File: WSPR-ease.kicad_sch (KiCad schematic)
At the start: 31 parts, among them J1 GNSS Ant, J2 Tx Ant, J3 USB_C_16P_Stacked, Q1 MMBF170, U1 ESP32-S3-WROOM-1, U2 NCP1117-3.3_SOT223, U3 ATGM336H-5N31

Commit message: Minor tweaks after submitting 001 build to pcbway
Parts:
- BT1: value CR1220 -> S8401-46; footprint Battery:Battery_Panasonic_CR1220-VCN_Vertical_CircularHoles -> S8401-46; symbol Device:Battery_Cell -> Library:S8401-46; LCSC (none) -> C5904513; Manufacturer_Name (none) -> Harwin; Manufacturer_Part_Number (none) -> S8401-46; Mouser Part Number (none) -> 855-S8401-46; Mouser Price/Stock (none) -> https://www.mouser.co.uk/ProductDetail/Harwin/S8401-46?qs=Q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
- C1: footprint Capacitor_SMD:C_0805_2012Metric -> Capacitor_SMD:C_0603_1608Metric
- C10: MFG Vishay -> (none); MPN MAL215097011E3 -> (none); Manufacturer_Name (none) -> Vishay; Mouser Part Number (none) -> MAL215097011E3
- J1, J2: LCSC (none) -> C496551
- J3: LCSC (none) -> C165948; MFG Korean Hroparts -> (none); MPN TYPE-C-31-M-12 -> (none); Manufacturer_Name (none) -> Korean Hroparts; Mouser Part Number (none) -> TYPE-C-31-M-12
- Q1: LCSC (none) -> C28871
- U1: value ESP32-S3-WROOM-1 -> ESP32-S3-WROOM-1-N8R8; LCSC (none) -> C2913204; Manufacturer_Name (none) -> Espressif; Mouser Part Number (none) -> ESP32-S3-WROOM-1-N8R8
- U3: LCSC (none) -> C90770
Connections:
- net GND: now also BT1.1 (-VE); no longer BT1.2 (-)
- net at U3.6 (V_BCKP): now also BT1.2, BT1.3; no longer BT1.1 (+)
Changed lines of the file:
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@@
 	)
 	(junction
+		(at 118.11 33.02)
+		(diameter 0)
+		(color 0 0 0 0)
+	)
+	(junction
 		(at 137.16 78.74)
 		(diameter 0)
@@
 	(wire
 		(pts
-			(xy 128.27 33.02) (xy 128.27 34.29)
+			(xy 143.51 33.02) (xy 143.51 34.29)
 		)
 		(stroke
@@
 	(wire
 		(pts
+			(xy 118.11 30.48) (xy 118.11 33.02)
+		)
+		(stroke
+			(width 0)
+			(type default)
+		)
+	)
+	(wire
+		(pts
 			(xy 88.9 63.5) (xy 90.17 63.5)
 		)
@@
 	(wire
 		(pts
+			(xy 119.38 30.48) (xy 118.11 30.48)
+		)
+		(stroke
+			(width 0)
+			(type default)
+		)
+	)
+	(wire
+		(pts
 			(xy 143.51 195.58) (xy 143.51 196.85)
 		)
@@
 	(wire
 		(pts
-			(xy 127 33.02) (xy 128.27 33.02)
+			(xy 142.24 33.02) (xy 143.51 33.02)
 		)
 		(stroke
@@
 			)
 		)
-		(property "Footprint" "Capacitor_SMD:C_0805_2012Metric"
+		(property "Footprint" "Capacitor_SMD:C_0603_1608Metric"
 			(at 32.7152 87.63 0)
 			(effects
@@
 	)
 	(symbol
-		(lib_id "Device:Battery_Cell")
-		(at 124.46 33.02 90)
+		(lib_id "Library:S8401-46")
+		(at 119.38 33.02 0)
 		(mirror x)
 		(unit 1)
@@
 		(fields_autoplaced yes)
 		(property "Reference" "BT1"
-			(at 122.6185 25.4 90)
+			(at 130.81 22.86 0)
 			(effects
 				(font
@@
 			)
 		)
-		(property "Value" "CR1220"
-			(at 122.6185 27.94 90)
+		(property "Value" "S8401-46"
+			(at 130.81 25.4 0)
 			(effects
 				(font
@@
 			)
 		)
-		(property "Footprint" "Battery:Battery_Panasonic_CR1220-VCN_Vertical_CircularHoles"
-			(at 122.936 33.02 90)
+		(property "Footprint" "S8401-46"
+			(at 138.43 -61.9 0)
 			(effects
 				(font
 					(size 1.27 1.27)
 				)
+				(justify left top)
 				(hide yes)
 			)
 		)
-		(property "Datasheet" "~"
-			(at 122.936 33.02 90)
+		(property "Datasheet" "https://cdn.harwin.com/pdfs/S8401.pdf"
+			(at 138.43 -161.9 0)
 			(effects
 				(font
 					(size 1.27 1.27)
 				)
+				(justify left top)
 				(hide yes)
 			)
 		)
-		(property "Description" "Single-cell battery"
-			(at 124.46 33.02 0)
+		(property "Description" "Coin Cell Battery Retainer, Vertical Throughboard, for CR2032 and BR2032 Coin Cell Batteries"
+			(at 119.38 33.02 0)
 			(effects
 				(font
@@
 			)
 		)
-		(property "LCSC" ""
-			(at 124.46 33.02 90)
+		(property "LCSC" "C5904513"
+			(at 119.38 33.02 90)
+			(effects
+				(font
+					(size 1.27 1.27)
+				)
+				(hide yes)
+			)
+		)
+		(property "Height" ""
+			(at 138.43 -361.9 0)
+			(effects
+				(font
+					(size 1.27 1.27)
+				)
+				(justify left top)
+				(hide yes)
+			)
+		)
+		(property "Mouser Part Number" "855-S8401-46"
+			(at 138.43 -461.9 0)
+			(effects
+				(font
+					(size 1.27 1.27)
+				)
+				(justify left top)
+				(hide yes)
+			)
+		)
+		(property "Mouser Price/Stock" "https://www.mouser.co.uk/ProductDetail/Harwin/S8401-46?qs=Qom7kyPojXaFNoCO9lxVnA%3D%3D"
+			(at 138.43 -561.9 0)
+			(effects
+				(font
+					(size 1.27 1.27)
+				)
+				(justify left top)
+				(hide yes)
+			)
+		)
+		(property "Manufacturer_Name" "Harwin"
+			(at 138.43 -661.9 0)
+			(effects
+				(font
+					(size 1.27 1.27)
+				)
+				(justify left top)
+				(hide yes)
+			)
+		)
+		(property "Manufacturer_Part_Number" "S8401-46"
+			(at 138.43 -761.9 0)
 			(effects
 				(font
 					(size 1.27 1.27)
 				)
+				(justify left top)
 				(hide yes)
 			)
@@
 		(pin "1"
 		)
+		(pin "3"
+		)
 		(instances
 			(project ""
@@
 			)
 		)
-		(property "MFG" "Korean Hroparts"
+		(property "MFG" ""
 			(at 227.33 66.04 0)
 			(effects
@@
 			)
 		)
-		(property "MPN" "TYPE-C-31-M-12"
+		(property "MPN" ""
 			(at 227.33 66.04 0)
 			(effects
@@
 			)
 		)
-		(property "LCSC" ""
+		(property "LCSC" "C165948"
+			(at 227.33 66.04 0)
+			(effects
+				(font
+					(size 1.27 1.27)
+				)
+				(hide yes)
+			)
+		)
+		(property "Manufacturer_Name" "Korean Hroparts"
+			(at 227.33 66.04 0)
+			(effects
+				(font
+					(size 1.27 1.27)
+				)
+				(hide yes)
+			)
+		)
+		(property "Mouser Part Number" "TYPE-C-31-M-12"
 			(at 227.33 66.04 0)
 			(effects
@@
 			)
 		)
-		(property "LCSC" ""
+		(property "LCSC" "C28871"
 			(at 41.91 76.2 0)
 			(effects
@@
 			)
 		)
-		(property "LCSC" ""
+		(property "LCSC" "C90770"
 			(at 134.62 58.42 0)
 			(effects
@@
 			)
 		)
-		(property "Datasheet" "~"
+		(property "Datasheet" "https://www.lcsc.com/datasheet/C496551.pdf"
 			(at 170.18 49.53 0)
 			(effects
@@
 			)
 		)
-		(property "Description" "small coaxial connector (BNC, SMA, SMB, SMC, Cinch/RCA, LEMO, ...)"
+		(property "Description" "1 Inner Bore SMA Board Side Elbow 50Ω 5.3mm Through Hole Coaxial Connector (RF) Assemblies RoHS"
 			(at 170.18 49.53 0)
 			(effects
@@
 			)
 		)
-		(property "LCSC" ""
+		(property "LCSC" "C496551"
 			(at 170.18 49.53 0)
 			(effects
@@
 			)
 		)
-		(property "Value" "ESP32-S3-WROOM-1"
+		(property "Value" "ESP32-S3-WROOM-1-N8R8"
 			(at 75.8033 48.26 0)
 			(effects
@@
 			)
 		)
-		(property "LCSC" ""
+		(property "LCSC" "C2913204"
+			(at 73.66 76.2 0)
+			(effects
+				(font
+					(size 1.27 1.27)
+				)
+				(hide yes)
+			)
+		)
+		(property "Manufacturer_Name" "Espressif"
+			(at 73.66 76.2 0)
+			(effects
+				(font
+					(size 1.27 1.27)
+				)
+				(hide yes)
+			)
+		)
+		(property "Mouser Part Number" "ESP32-S3-WROOM-1-N8R8"
 			(at 73.66 76.2 0)
 			(effects
@@
 			)
 		)
-		(property "Datasheet" "~"
+		(property "Datasheet" "https://www.lcsc.com/datasheet/C496551.pdf"
 			(at 195.58 142.24 0)
 			(effects
@@
 			)
 		)
-		(property "Description" "small coaxial connector (BNC, SMA, SMB, SMC, Cinch/RCA, LEMO, ...)"
+		(property "Description" "1 Inner Bore SMA Board Side Elbow 50Ω 5.3mm Through Hole Coaxial Connector (RF) Assemblies RoHS"
 			(at 195.58 142.24 0)
 			(effects
@@
 			)
 		)
-		(property "LCSC" ""
+		(property "LCSC" "C496551"
 			(at 195.58 142.24 0)
 			(effects
@@
 	(symbol
 		(lib_id "power:GND")
-		(at 128.27 34.29 0)
+		(at 143.51 34.29 0)
 		(unit 1)
 		(exclude_from_sim no)
@@
 		(fields_autoplaced yes)
 		(property "Reference" "#PWR012"
-			(at 128.27 40.64 0)
+			(at 143.51 40.64 0)
 			(effects
 				(font
@@
 		)
 		(property "Value" "GND"
-			(at 128.27 39.37 0)
+			(at 143.51 39.37 0)
 			(effects
 				(font
@@
 		)
 		(property "Footprint" ""
-			(at 128.27 34.29 0)
+			(at 143.51 34.29 0)
 			(effects
 				(font
@@
 		)
 		(property "Datasheet" ""
-			(at 128.27 34.29 0)
+			(at 143.51 34.29 0)
 			(effects
 				(font
@@
 		)
 		(property "Description" "Power symbol creates a global label with name \"GND\" , ground"
-			(at 128.27 34.29 0)
+			(at 143.51 34.29 0)
 			(effects
 				(font
@@
 			)
 		)
-		(property "MFG" "Vishay"
+		(property "MFG" ""
+			(at 262.89 63.5 0)
+			(effects
+				(font
+					(size 1.27 1.27)
+				)
+				(hide yes)
+			)
+		)
+		(property "MPN" ""
+			(at 262.89 63.5 0)
+			(effects
+				(font
+					(size 1.27 1.27)
+				)
+				(hide yes)
+			)
+		)
+		(property "Manufacturer_Name" "Vishay"
 			(at 262.89 63.5 0)
 			(effects
@@
 			)
 		)
-		(property "MPN" "MAL215097011E3"
+		(property "Mouser Part Number" "MAL215097011E3"
 			(at 262.89 63.5 0)
 			(effects

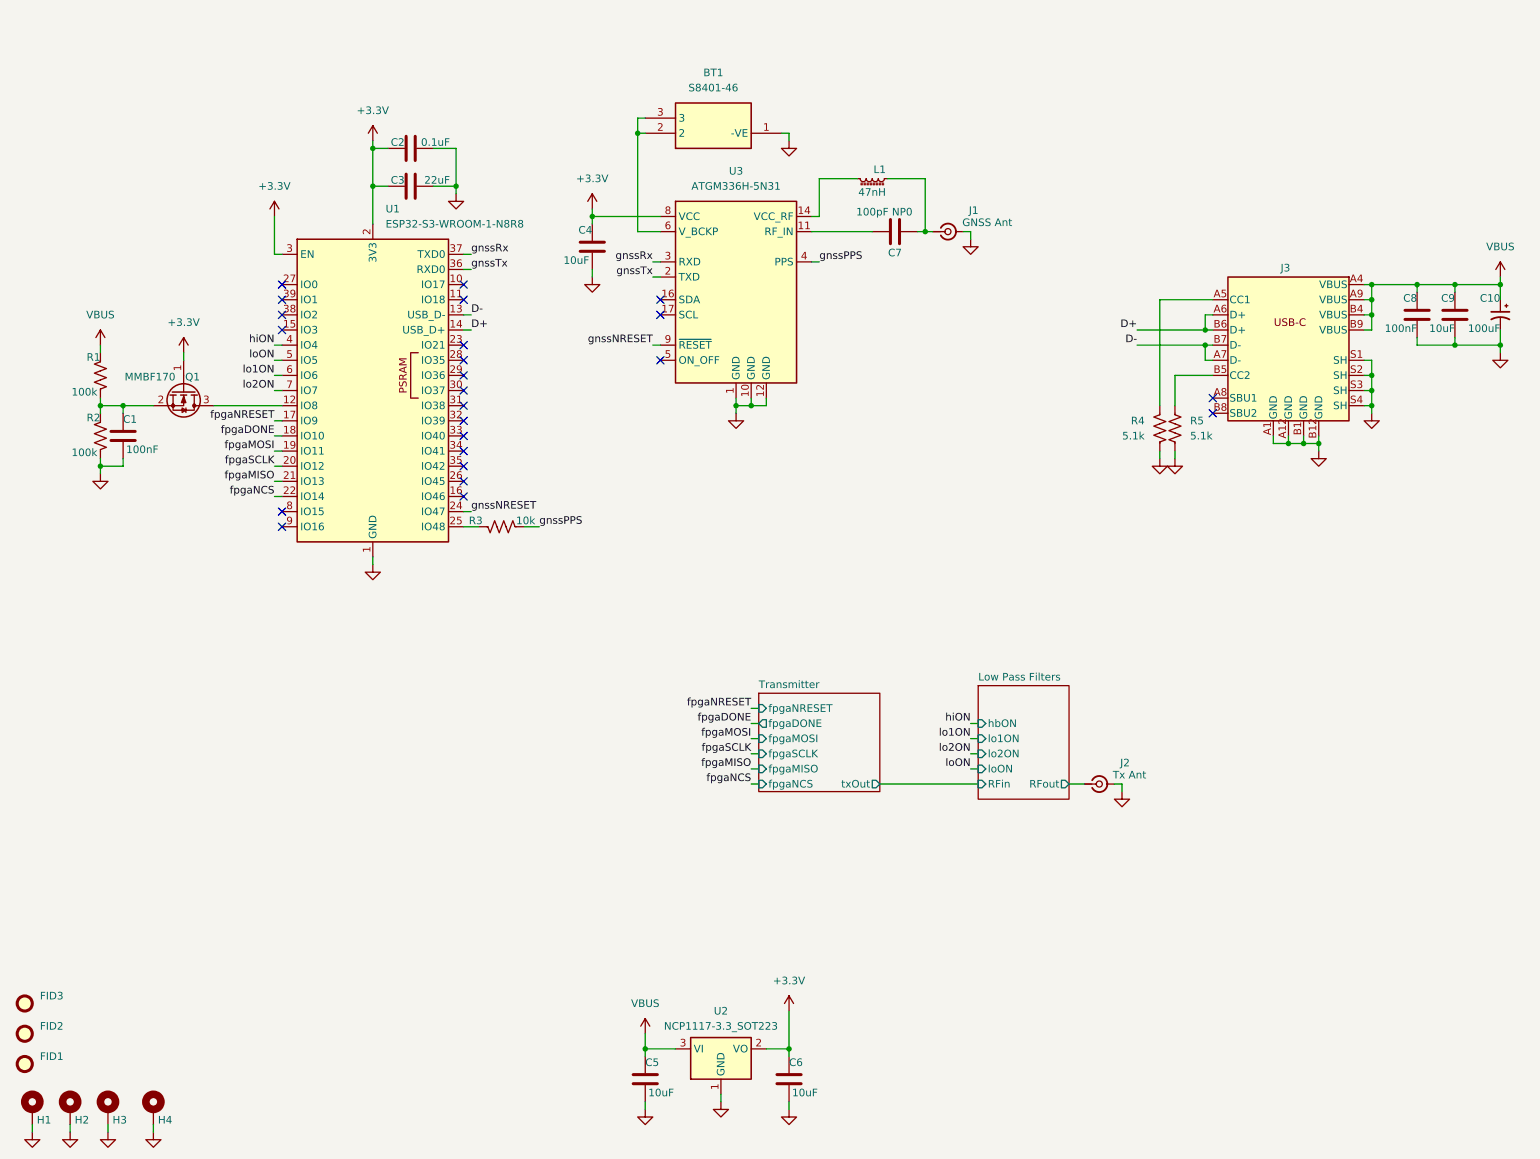
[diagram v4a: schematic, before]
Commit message: Submitted to PCBway (I had to update BOM after oops)
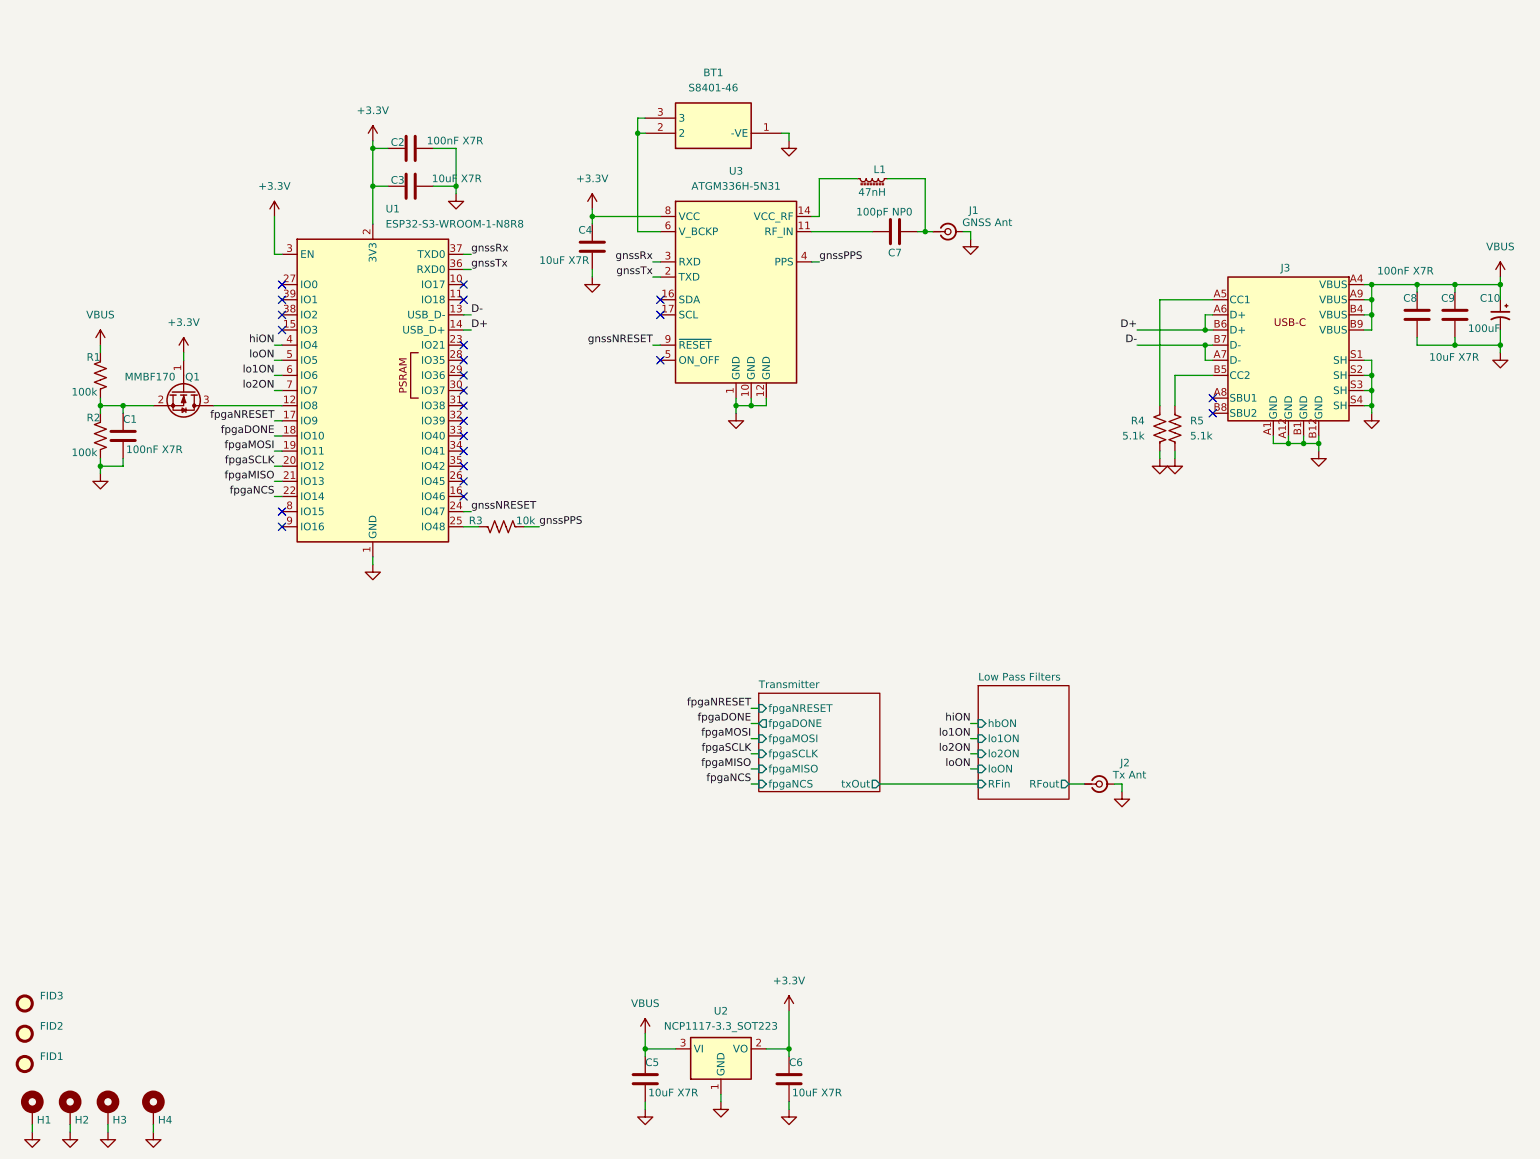
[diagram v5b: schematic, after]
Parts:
- C1, C8: value 100nF -> 100nF X7R; LCSC (none) -> C14663
- C2: value 0.1uF -> 100nF X7R; LCSC (none) -> C14663
- C3: value 22uF -> 10uF X7R; LCSC (none) -> C19702
- C4, C5, C6, C9: value 10uF -> 10uF X7R; LCSC (none) -> C32635
- C7: LCSC (none) -> C14665
- FID1, FID2, FID3, H1, H2, H3, H4: LCSC (none) -> DNP
- L1: LCSC (none) -> C98076
- R1, R2: LCSC (none) -> C7311067
- R3: LCSC (none) -> C2930027
- R4, R5: LCSC (none) -> C2907114
- U2: LCSC (none) -> C26537
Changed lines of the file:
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@@
 			)
 		)
-		(property "Value" "100nF"
+		(property "Value" "100nF X7R"
 			(at 32.258 86.106 0)
 			(effects
@@
 			)
 		)
-		(property "LCSC" ""
+		(property "LCSC" "C14663"
 			(at 31.75 83.82 0)
 			(effects
@@
 			)
 		)
-		(property "LCSC" ""
+		(property "LCSC" "C7311067"
 			(at 27.94 73.66 0)
 			(effects
@@
 			)
 		)
+		(property "LCSC" "DNP"
+			(at 29.21 196.85 0)
+			(effects
+				(font
+					(size 1.27 1.27)
+				)
+				(hide yes)
+			)
+		)
 		(pin "1"
 		)
@@
 			)
 		)
-		(property "Value" "100nF"
-			(at 248.92 65.786 0)
+		(property "Value" "100nF X7R"
+			(at 251.714 56.134 0)
 			(effects
 				(font
@@
 			)
 		)
-		(property "LCSC" ""
+		(property "LCSC" "C14663"
 			(at 248.92 63.5 0)
 			(effects
@@
 			)
 		)
-		(property "LCSC" ""
+		(property "LCSC" "C14665"
 			(at 161.29 49.53 90)
 			(effects
@@
 			)
 		)
+		(property "LCSC" "DNP"
+			(at 16.51 196.85 0)
+			(effects
+				(font
+					(size 1.27 1.27)
+				)
+				(hide yes)
+			)
+		)
 		(pin "1"
 		)
@@
 			)
 		)
+		(property "LCSC" "DNP"
+			(at 15.24 189.23 0)
+			(effects
+				(font
+					(size 1.27 1.27)
+				)
+				(hide yes)
+			)
+		)
 		(instances
 			(project ""
@@
 			)
 		)
-		(property "Value" "10uF"
+		(property "Value" "10uF X7R"
 			(at 144.018 194.056 0)
 			(effects
@@
 			)
 		)
-		(property "LCSC" ""
+		(property "LCSC" "C32635"
 			(at 143.51 191.77 0)
 			(effects
@@
 			)
 		)
-		(property "LCSC" ""
+		(property "LCSC" "C98076"
 			(at 157.48 40.64 90)
 			(effects
@@
 			)
 		)
-		(property "LCSC" ""
+		(property "LCSC" "C26537"
 			(at 132.08 186.69 0)
 			(effects
@@
 			)
 		)
+		(property "LCSC" "DNP"
+			(at 36.83 196.85 0)
+			(effects
+				(font
+					(size 1.27 1.27)
+				)
+				(hide yes)
+			)
+		)
 		(pin "1"
 		)
@@
 			)
 		)
+		(property "LCSC" "DNP"
+			(at 15.24 179.07 0)
+			(effects
+				(font
+					(size 1.27 1.27)
+				)
+				(hide yes)
+			)
+		)
 		(instances
 			(project "WSPR-ease"
@@
 			)
 		)
-		(property "Value" "10uF"
-			(at 255.27 65.786 0)
+		(property "Value" "10uF X7R"
+			(at 259.334 70.612 0)
 			(effects
 				(font
@@
 			)
 		)
-		(property "LCSC" ""
+		(property "LCSC" "C32635"
 			(at 255.27 63.5 0)
 			(effects
@@
 			)
 		)
-		(property "LCSC" ""
+		(property "LCSC" "C2907114"
 			(at 208.28 82.55 0)
 			(effects
@@
 			)
 		)
-		(property "LCSC" ""
+		(property "LCSC" "C7311067"
 			(at 27.94 83.82 0)
 			(effects
@@
 			)
 		)
-		(property "Value" "10uF"
+		(property "Value" "10uF X7R"
 			(at 119.888 194.056 0)
 			(effects
@@
 			)
 		)
-		(property "LCSC" ""
+		(property "LCSC" "C32635"
 			(at 119.38 191.77 0)
 			(effects
@@
 			)
 		)
-		(property "LCSC" ""
+		(property "LCSC" "C2930027"
 			(at 95.25 99.06 90)
 			(effects
@@
 			)
 		)
-		(property "Value" "22uF"
-			(at 86.614 40.894 90)
+		(property "Value" "10uF X7R"
+			(at 91.948 40.64 90)
 			(effects
 				(font
@@
 			)
 		)
-		(property "LCSC" ""
+		(property "LCSC" "C19702"
 			(at 80.01 41.91 90)
 			(effects
@@
 			)
 		)
-		(property "Value" "0.1uF"
-			(at 86.614 34.544 90)
+		(property "Value" "100nF X7R"
+			(at 92.202 34.29 90)
 			(effects
 				(font
@@
 			)
 		)
-		(property "LCSC" ""
+		(property "LCSC" "C14663"
 			(at 80.01 35.56 90)
 			(effects
@@
 			)
 		)
+		(property "LCSC" "DNP"
+			(at 15.24 184.15 0)
+			(effects
+				(font
+					(size 1.27 1.27)
+				)
+				(hide yes)
+			)
+		)
 		(instances
 			(project "WSPR-ease"
@@
 			)
 		)
-		(property "Value" "10uF"
+		(property "Value" "10uF X7R"
 			(at 109.982 54.356 0)
 			(effects
@@
 			)
 		)
-		(property "LCSC" ""
+		(property "LCSC" "C32635"
 			(at 110.49 52.07 0)
 			(effects
@@
 			)
 		)
-		(property "LCSC" ""
+		(property "LCSC" "C2907114"
 			(at 205.74 82.55 0)
 			(effects
@@
 			(at 22.86 196.85 0)
 			(effects
+				(font
+					(size 1.27 1.27)
+				)
+				(hide yes)
+			)
+		)
+		(property "LCSC" "DNP"
+			(at 22.86 196.85 0)
+			(effects
